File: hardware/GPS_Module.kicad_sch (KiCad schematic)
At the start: 10 parts, among them J6 Conn_01x04_Pin, J7 Conn_01x04_Pin, U4 SAM-M8Q

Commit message: Fix several DRC errors & add all 3D models
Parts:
- J6, J7: footprint Connector_JST:JST_XA_B04B-XASK-1_1x04_P2.50mm_Vertical -> Connector_JST:JST_XH_B4B-XH-A_1x04_P2.50mm_Vertical
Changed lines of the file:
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@@
 			)
 		)
-		(property "Footprint" "Connector_JST:JST_XA_B04B-XASK-1_1x04_P2.50mm_Vertical"
+		(property "Footprint" "Connector_JST:JST_XH_B4B-XH-A_1x04_P2.50mm_Vertical"
 			(at 99.06 144.78 0)
 			(effects
@@
 			)
 		)
-		(property "Footprint" "Connector_JST:JST_XA_B04B-XASK-1_1x04_P2.50mm_Vertical"
+		(property "Footprint" "Connector_JST:JST_XH_B4B-XH-A_1x04_P2.50mm_Vertical"
 			(at 129.54 144.78 0)
 			(effects

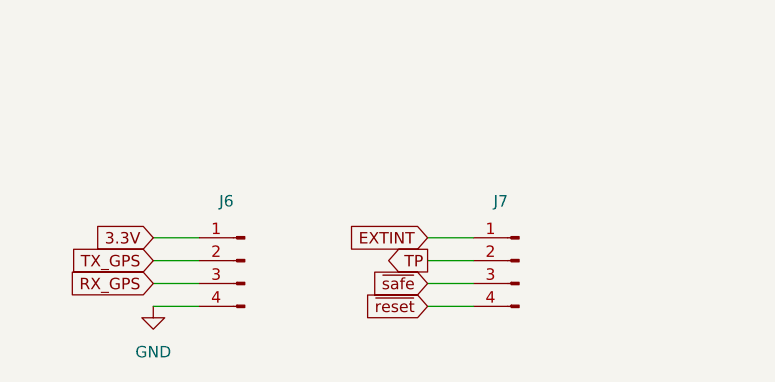
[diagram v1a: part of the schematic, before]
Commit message: Finished optimal placement & adapted/fixed schematic
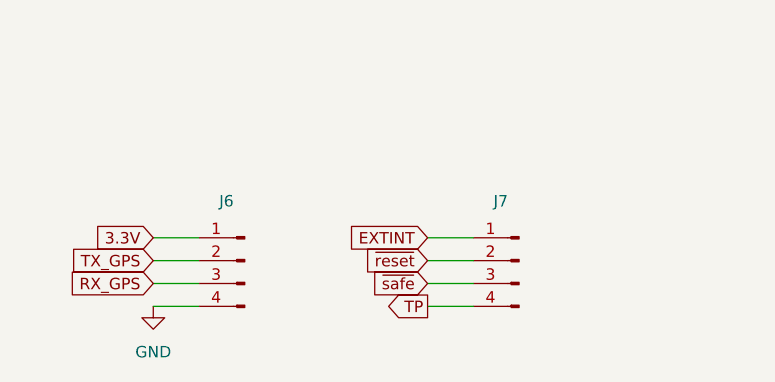
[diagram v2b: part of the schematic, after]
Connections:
- net TP: now also J7.4 (Pin_4); no longer J7.2 (Pin_2)
- net ~{reset}: now also J7.2 (Pin_2); no longer J7.4 (Pin_4)
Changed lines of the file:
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@@
 	(global_label "~{reset}"
 		(shape input)
-		(at 119.38 149.86 180)
+		(at 119.38 144.78 180)
 		(fields_autoplaced yes)
 		(effects
@@
 		)
 		(property "Intersheetrefs" "${INTERSHEET_REFS}"
-			(at 111.6776 149.86 0)
+			(at 111.6776 144.78 0)
 			(effects
 				(font
@@
 	(global_label "TP"
 		(shape output)
-		(at 119.38 144.78 180)
+		(at 119.38 149.86 180)
 		(fields_autoplaced yes)
 		(effects
@@
 		)
 		(property "Intersheetrefs" "${INTERSHEET_REFS}"
-			(at 114.1572 144.78 0)
+			(at 114.1572 149.86 0)
 			(effects
 				(font

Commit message: Find all remaining components on JLCPCB
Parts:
- C7: JLCPCB Part # (none) -> C29936; Package (none) -> 0603
- D2: JLCPCB Part # (none) -> C7470862; Package (none) -> 0603
- J6, J7: JLCPCB Part # (none) -> C161871; Package (none) -> Plugin,P=2.5mm
- R10: JLCPCB Part # (none) -> C22548; Package (none) -> 0603
- R11, R12: JLCPCB Part # (none) -> C114669; Package (none) -> 0603
- R13, R14: JLCPCB Part # (none) -> C107701; Package (none) -> 0603
- U4: JLCPCB Part # (none) -> C5447387; Package (none) -> SMD-20P,15x15mm
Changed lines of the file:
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@@
 			)
 		)
-		(property "Description" "Resistor"
+		(property "Description" "RC0603FR-07470RL 100mW 470Ω 75V Thick Film Resistor ±1% 0603"
+			(at 173.99 77.47 0)
+			(effects
+				(font
+					(size 1.27 1.27)
+				)
+				(hide yes)
+			)
+		)
+		(property "JLCPCB Part #" "C114669"
+			(at 173.99 77.47 0)
+			(effects
+				(font
+					(size 1.27 1.27)
+				)
+				(hide yes)
+			)
+		)
+		(property "Package" "0603"
 			(at 173.99 77.47 0)
 			(effects
@@
 			)
 		)
-		(property "Description" "Resistor"
+		(property "Description" "RC0603FR-0722RL 100mW 22Ω 75V Thick Film Resistor ±1% 0603"
+			(at 173.99 87.63 0)
+			(effects
+				(font
+					(size 1.27 1.27)
+				)
+				(hide yes)
+			)
+		)
+		(property "JLCPCB Part #" "C107701"
+			(at 173.99 87.63 0)
+			(effects
+				(font
+					(size 1.27 1.27)
+				)
+				(hide yes)
+			)
+		)
+		(property "Package" "0603"
 			(at 173.99 87.63 0)
 			(effects
@@
 			)
 		)
-		(property "Description" "Resistor"
+		(property "Description" "RC0603FR-07470RL 100mW 470Ω 75V Thick Film Resistor ±1% 0603"
+			(at 173.99 80.01 0)
+			(effects
+				(font
+					(size 1.27 1.27)
+				)
+				(hide yes)
+			)
+		)
+		(property "JLCPCB Part #" "C114669"
+			(at 173.99 80.01 0)
+			(effects
+				(font
+					(size 1.27 1.27)
+				)
+				(hide yes)
+			)
+		)
+		(property "Package" "0603"
 			(at 173.99 80.01 0)
 			(effects
@@
 			)
 		)
-		(property "Description" "Resistor"
+		(property "Description" "RC0603FR-071KL 100mW 1kΩ 75V Thick Film Resistor ±1% 0603"
+			(at 78.74 71.12 0)
+			(effects
+				(font
+					(size 1.27 1.27)
+				)
+				(hide yes)
+			)
+		)
+		(property "JLCPCB Part #" "C22548"
+			(at 78.74 71.12 0)
+			(effects
+				(font
+					(size 1.27 1.27)
+				)
+				(hide yes)
+			)
+		)
+		(property "Package" "0603"
 			(at 78.74 71.12 0)
 			(effects
@@
 			)
 		)
-		(property "Description" "Resistor"
+		(property "Description" "RC0603FR-0722RL 100mW 22Ω 75V Thick Film Resistor ±1% 0603"
+			(at 173.99 85.09 0)
+			(effects
+				(font
+					(size 1.27 1.27)
+				)
+				(hide yes)
+			)
+		)
+		(property "JLCPCB Part #" "C107701"
+			(at 173.99 85.09 0)
+			(effects
+				(font
+					(size 1.27 1.27)
+				)
+				(hide yes)
+			)
+		)
+		(property "Package" "0603"
 			(at 173.99 85.09 0)
 			(effects
@@
 			)
 		)
-		(property "Description" "Generic connector, single row, 01x04, script generated"
+		(property "Description" "B4B-XH-AM(LF)(SN) 1x4P 2.5mm JST connector"
+			(at 99.06 144.78 0)
+			(effects
+				(font
+					(size 1.27 1.27)
+				)
+				(hide yes)
+			)
+		)
+		(property "JLCPCB Part #" "C161871"
+			(at 99.06 144.78 0)
+			(effects
+				(font
+					(size 1.27 1.27)
+				)
+				(hide yes)
+			)
+		)
+		(property "Package" "Plugin,P=2.5mm"
 			(at 99.06 144.78 0)
 			(effects
@@
 			)
 		)
-		(property "Description" "Light emitting diode"
+		(property "Description" "MEIHUA MHT192DUGCT LED 2.3V~2.8V 518nm 565mcd 5mA 60mW Green"
+			(at 78.74 81.28 0)
+			(effects
+				(font
+					(size 1.27 1.27)
+				)
+				(hide yes)
+			)
+		)
+		(property "JLCPCB Part #" "C7470862"
+			(at 78.74 81.28 0)
+			(effects
+				(font
+					(size 1.27 1.27)
+				)
+				(hide yes)
+			)
+		)
+		(property "Package" "0603"
 			(at 78.74 81.28 0)
 			(effects
@@
 			)
 		)
-		(property "Description" "Generic connector, single row, 01x04, script generated"
+		(property "Description" "B4B-XH-AM(LF)(SN) 1x4P 2.5mm JST connector"
+			(at 129.54 144.78 0)
+			(effects
+				(font
+					(size 1.27 1.27)
+				)
+				(hide yes)
+			)
+		)
+		(property "JLCPCB Part #" "C161871"
+			(at 129.54 144.78 0)
+			(effects
+				(font
+					(size 1.27 1.27)
+				)
+				(hide yes)
+			)
+		)
+		(property "Package" "Plugin,P=2.5mm"
 			(at 129.54 144.78 0)
 			(effects
@@
 			)
 		)
+		(property "JLCPCB Part #" "C5447387"
+			(at 152.4 82.55 0)
+			(effects
+				(font
+					(size 1.27 1.27)
+				)
+				(hide yes)
+			)
+		)
+		(property "Package" "SMD-20P,15x15mm"
+			(at 152.4 82.55 0)
+			(effects
+				(font
+					(size 1.27 1.27)
+				)
+				(hide yes)
+			)
+		)
 		(pin "17"
 		)
@@
 			)
 		)
-		(property "Description" "Unpolarized capacitor"
+		(property "Description" "CL10B105KA8NNNC 1uF 25V X7R ±10% 0603 Multilayer Ceramic Capacitor"
 			(at 96.52 82.55 0)
 			(effects
+				(font
+					(size 1.27 1.27)
+				)
+				(hide yes)
+			)
+		)
+		(property "JLCPCB Part #" "C29936"
+			(at 96.52 82.55 0)
+			(effects
+				(font
+					(size 1.27 1.27)
+				)
+				(hide yes)
+			)
+		)
+		(property "Package" "0603"
+			(at 96.52 82.55 0)
+			(effects
